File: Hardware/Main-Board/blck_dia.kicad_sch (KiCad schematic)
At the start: 8 parts, among them J1 Conn_01x06, U3 W25Q128JVS, U4 RP2040, Y1 ABM8-272-T3

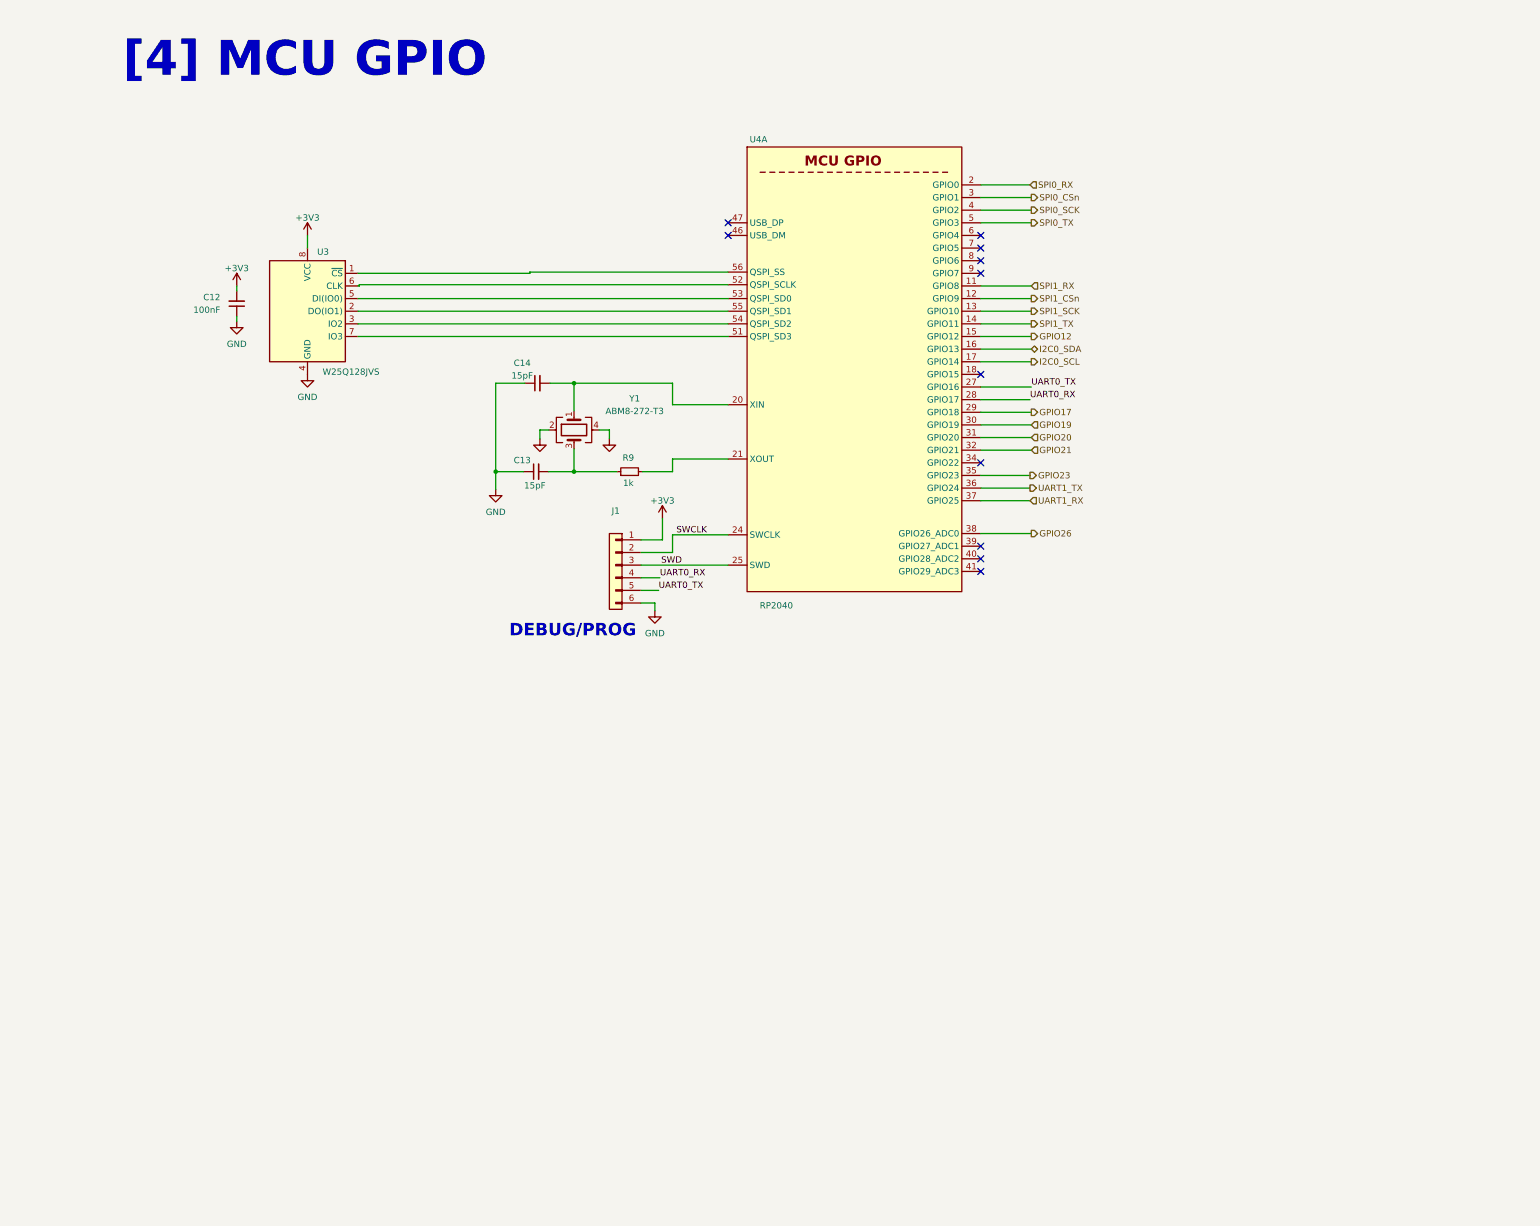
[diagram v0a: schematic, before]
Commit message: Done with main board design, and camera interconnect in progress
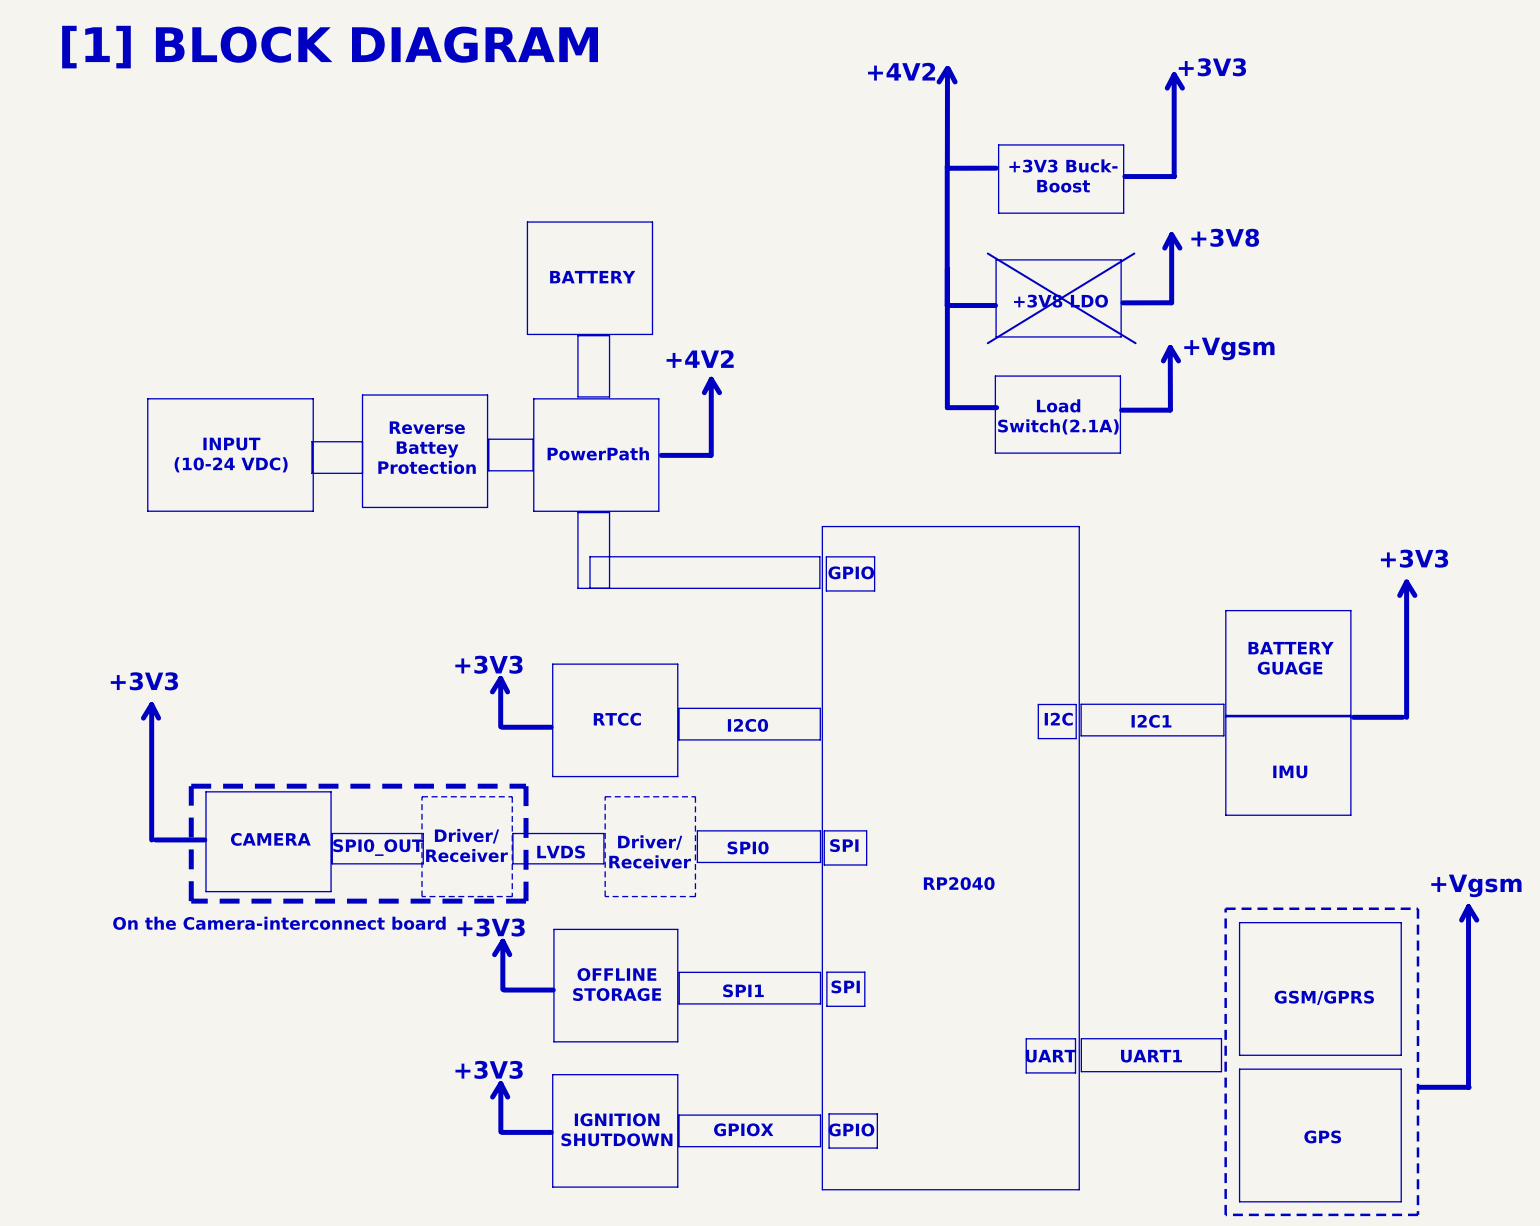
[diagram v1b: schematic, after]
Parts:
- removed C12: 100nF, Capacitor_SMD:C_0402_1005Metric, symbol Device:C_Small
- removed C13, C14: 15pF, Capacitor_SMD:C_0402_1005Metric, symbol Device:C_Small
- removed J1: Conn_01x06, Connector_PinHeader_2.54mm:PinHeader_2x03_P2.54mm_Vertical, symbol Connector_Generic:Conn_01x06
- removed R9: 1k, Resistor_SMD:R_0402_1005Metric, symbol Device:R_Small
- removed U3: W25Q128JVS, Package_SO:SOIC-8_5.23x5.23mm_P1.27mm, symbol Memory_Flash:W25Q128JVS
- removed U4: RP2040, Package_DFN_QFN:QFN-56-1EP_7x7mm_P0.4mm_EP3.2x3.2mm, symbol MCU_RaspberryPi:RP2040
- removed Y1: ABM8-272-T3, ABM8_272_T3:ABM8-272-T3_ABR, symbol Device:Crystal_GND24
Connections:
- no-connect marks 11 -> 0
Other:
- note added: "+3V3"
- note added: "+3V3 Buck- Boost"
- note added: "+3V8"
- note added: "+3V8 LDO"
- note added: "+4V2"
- note added: "+Vgsm"
- note added: "BATTERY"
- note added: "BATTERY GUAGE"
- note added: "CAMERA"
- note added: "Driver/ Receiver"
- note added: "GPIO"
- note added: "GPIOX"
- note added: "GPS"
- note added: "GSM/GPRS"
- note added: "I2C"
- note added: "I2C0"
- note added: "I2C1"
- note added: "IGNITION SHUTDOWN"
- note added: "IMU"
- note added: "INPUT (10-24 VDC)"
- note added: "LVDS"
- note added: "Load Switch(2.1A)"
- note added: "OFFLINE STORAGE"
- note added: "On the Camera-interconnect board"
- note added: "PowerPath"
- note added: "RP2040"
- note added: "RTCC"
- note added: "Reverse Battey Protection"
- note added: "SPI"
- note added: "SPI0"
- note added: "SPI0_OUT"
- note added: "SPI1"
- note added: "UART"
- note added: "UART1"
- note added: "[1] BLOCK DIAGRAM"
- note removed: "DEBUG/PROG"
- note removed: "[4] MCU GPIO"
